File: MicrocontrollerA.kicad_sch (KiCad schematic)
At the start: 35 parts, among them J1 SWD Connector, J13 USB_B_Micro, SW1 SW_Push, SW2 SW_SPDT, SW3 SW_SPDT, U1 STM32F446RCTx, U5 TVS0500DRV, Y1 25 MHz

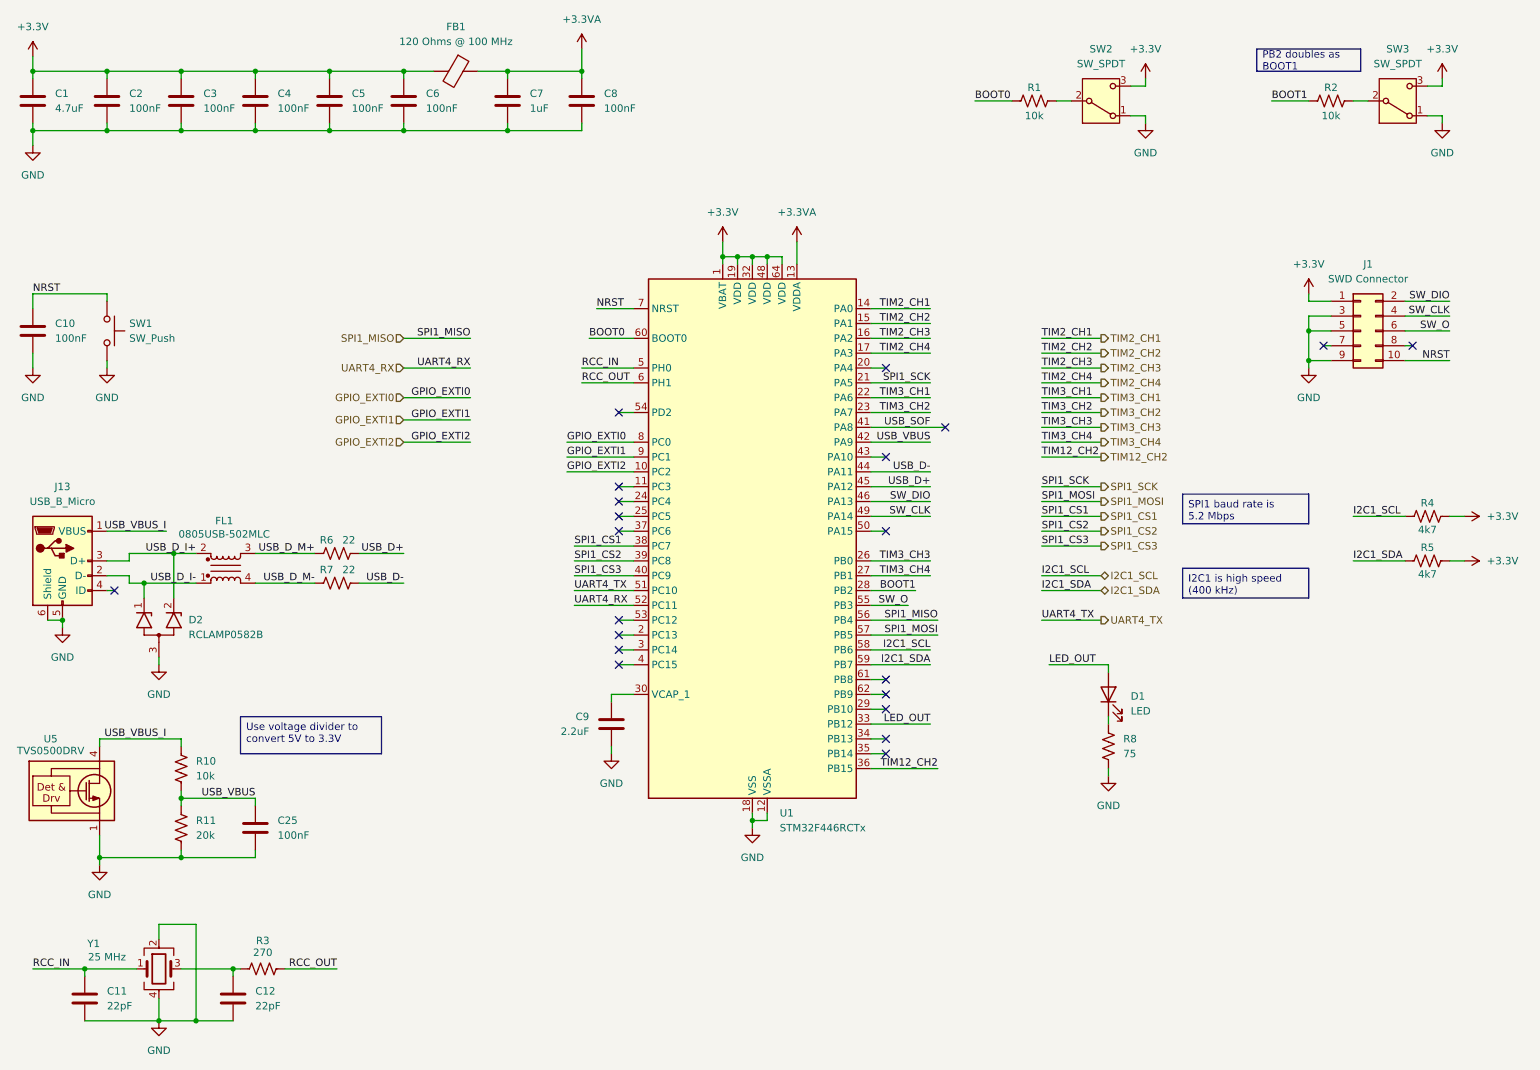
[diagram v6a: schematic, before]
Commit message: Add second SPI pins and connector
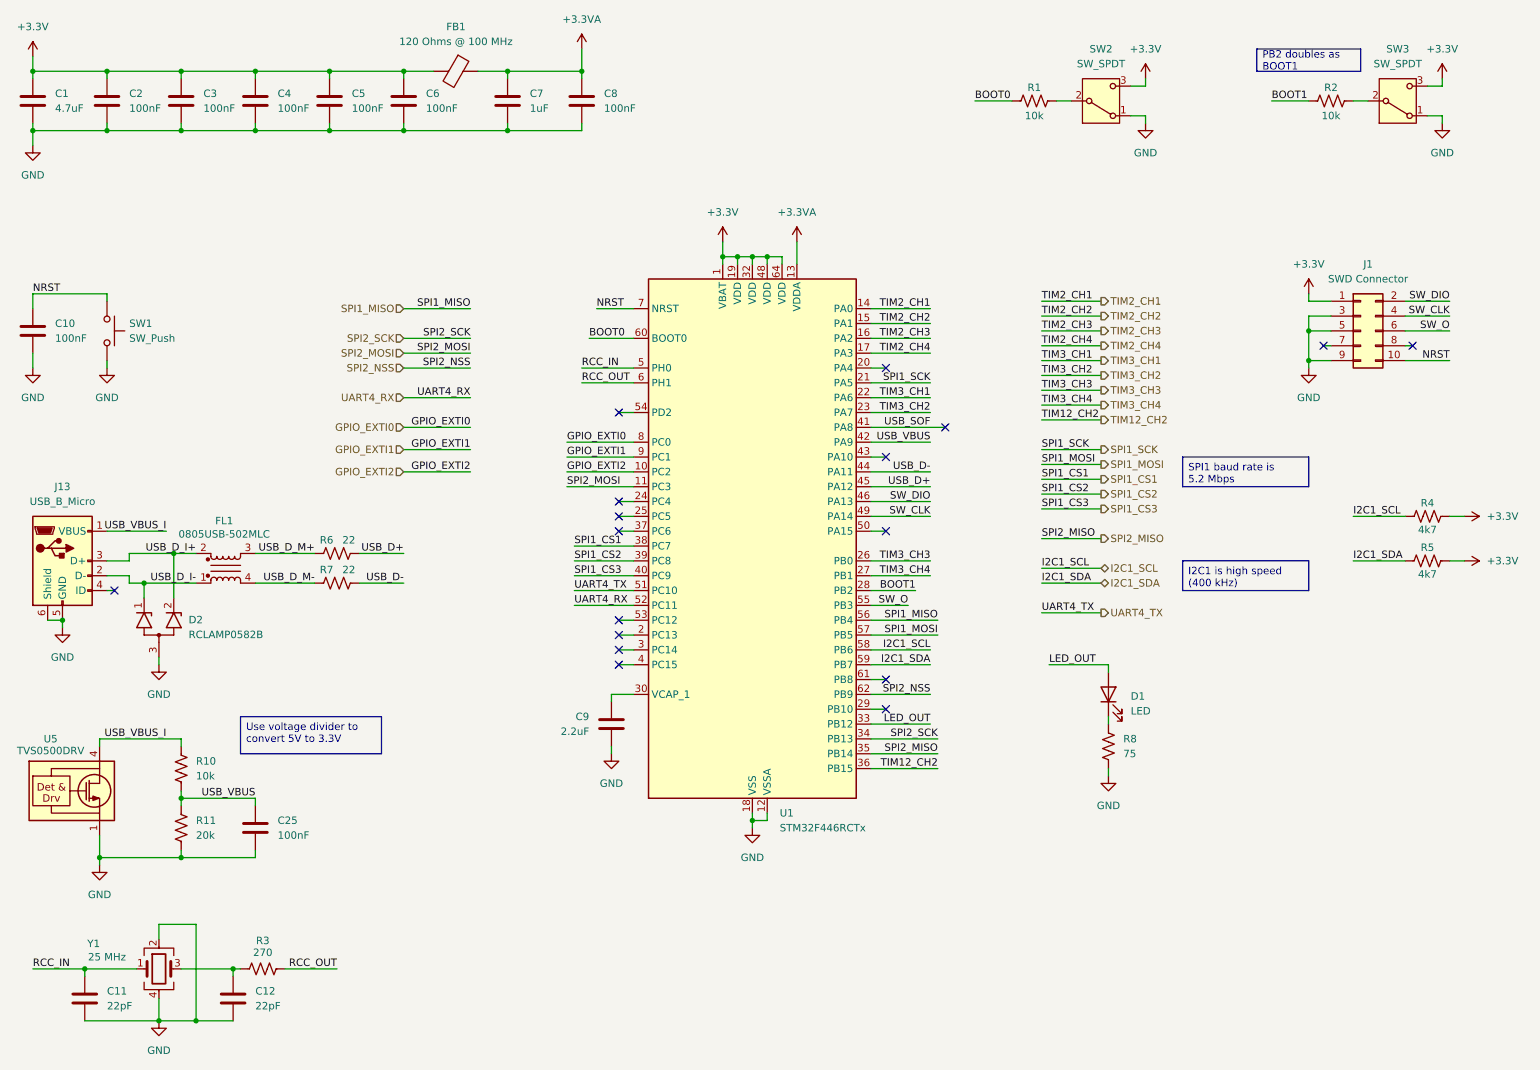
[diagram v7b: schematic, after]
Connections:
- net SPI2_MOSI: now reaches U1.11 (PC3)
- net SPI2_SCK: now reaches U1.34 (PB13)
- net SPI2_MISO: now reaches U1.35 (PB14)
- net SPI2_NSS: now reaches U1.62 (PB9)
- no-connect marks 21 -> 17

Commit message: Add second UART interface and connector
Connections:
- net UART5_TX: now reaches U1.53 (PC12)
- net UART5_RX: now reaches U1.54 (PD2)
- no-connect marks 17 -> 15
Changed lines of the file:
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@@
 	(title_block
 		(title "MCU A - STM32F446RCT6")
-		(date "2026-01-27")
+		(date "2026-01-28")
 		(rev "B")
 		(company "CU Boulder Senior Design Team 29 - Xu Lab")
@@
 	)
 	(no_connect
-		(at 125.73 83.82)
-	)
-	(no_connect
 		(at 261.62 72.39)
 	)
@@
 	)
 	(no_connect
-		(at 125.73 119.38)
-	)
-	(no_connect
 		(at 181.61 86.36)
 	)
@@
 	(wire
 		(pts
-			(xy 88.9 90.17) (xy 100.33 90.17)
+			(xy 88.9 92.71) (xy 100.33 92.71)
 		)
 		(stroke
@@
 	(wire
 		(pts
-			(xy 88.9 93.98) (xy 100.33 93.98)
+			(xy 88.9 96.52) (xy 100.33 96.52)
 		)
 		(stroke
@@
 	(wire
 		(pts
+			(xy 198.12 120.65) (xy 208.28 120.65)
+		)
+		(stroke
+			(width 0)
+			(type default)
+		)
+	)
+	(wire
+		(pts
 			(xy 168.91 111.76) (xy 179.07 111.76)
 		)
@@
 	(wire
 		(pts
-			(xy 125.73 83.82) (xy 128.27 83.82)
-		)
-		(stroke
-			(width 0)
-			(type default)
-		)
-	)
-	(wire
-		(pts
 			(xy 118.11 116.84) (xy 128.27 116.84)
 		)
@@
 	(wire
 		(pts
-			(xy 125.73 119.38) (xy 128.27 119.38)
-		)
-		(stroke
-			(width 0)
-			(type default)
-		)
-	)
-	(wire
-		(pts
 			(xy 125.73 127) (xy 128.27 127)
 		)
@@
 	(wire
 		(pts
+			(xy 118.11 83.82) (xy 128.27 83.82)
+		)
+		(stroke
+			(width 0)
+			(type default)
+		)
+	)
+	(wire
+		(pts
 			(xy 50.8 158.75) (xy 50.8 160.02)
 		)
@@
 	(wire
 		(pts
+			(xy 118.11 119.38) (xy 128.27 119.38)
+		)
+		(stroke
+			(width 0)
+			(type default)
+		)
+	)
+	(wire
+		(pts
 			(xy 260.35 72.39) (xy 261.62 72.39)
 		)
@@
 	(wire
 		(pts
-			(xy 88.9 86.36) (xy 100.33 86.36)
+			(xy 88.9 83.82) (xy 100.33 83.82)
+		)
+		(stroke
+			(width 0)
+			(type default)
+		)
+	)
+	(wire
+		(pts
+			(xy 88.9 88.9) (xy 100.33 88.9)
 		)
 		(stroke
@@
 	)
 	(label "GPIO_EXTI2"
-		(at 100.33 93.98 180)
+		(at 100.33 96.52 180)
 		(effects
 			(font
@@
 		)
 	)
+	(label "UART5_RX"
+		(at 100.33 83.82 180)
+		(effects
+			(font
+				(size 1.27 1.27)
+			)
+			(justify right bottom)
+		)
+	)
 	(label "TIM3_CH4"
 		(at 179.07 111.76 180)
@@
 		)
 	)
+	(label "UART5_TX"
+		(at 198.12 120.65 0)
+		(effects
+			(font
+				(size 1.27 1.27)
+			)
+			(justify left bottom)
+		)
+	)
 	(label "USB_D-"
 		(at 179.07 93.98 180)
@@
 		)
 	)
+	(label "UART5_RX"
+		(at 118.11 83.82 0)
+		(effects
+			(font
+				(size 1.27 1.27)
+			)
+			(justify left bottom)
+		)
+	)
 	(label "TIM3_CH2"
 		(at 198.12 77.47 0)
@@
 	)
 	(label "GPIO_EXTI0"
-		(at 100.33 86.36 180)
+		(at 100.33 88.9 180)
 		(effects
 			(font
@@
 	)
 	(label "GPIO_EXTI1"
-		(at 100.33 90.17 180)
+		(at 100.33 92.71 180)
 		(effects
 			(font
@@
 		)
 	)
+	(label "UART5_TX"
+		(at 118.11 119.38 0)
+		(effects
+			(font
+				(size 1.27 1.27)
+			)
+			(justify left bottom)
+		)
+	)
 	(label "TIM3_CH4"
 		(at 198.12 82.55 0)
@@
 		)
 	)
+	(hierarchical_label "UART5_RX"
+		(shape input)
+		(at 88.9 83.82 180)
+		(effects
+			(font
+				(size 1.27 1.27)
+			)
+			(justify right)
+		)
+	)
 	(hierarchical_label "TIM2_CH1"
 		(shape output)
@@
 	(hierarchical_label "GPIO_EXTI1"
 		(shape input)
-		(at 88.9 90.17 180)
+		(at 88.9 92.71 180)
 		(effects
 			(font
@@
 	(hierarchical_label "GPIO_EXTI2"
 		(shape input)
-		(at 88.9 93.98 180)
+		(at 88.9 96.52 180)
 		(effects
 			(font
@@
 		)
 	)
+	(hierarchical_label "UART5_TX"
+		(shape output)
+		(at 208.28 120.65 0)
+		(effects
+			(font
+				(size 1.27 1.27)
+			)
+			(justify left)
+		)
+	)
 	(hierarchical_label "UART4_TX"
 		(shape output)
@@
 	(hierarchical_label "GPIO_EXTI0"
 		(shape input)
-		(at 88.9 86.36 180)
+		(at 88.9 88.9 180)
 		(effects
 			(font
